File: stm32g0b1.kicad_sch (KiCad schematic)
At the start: 1 part, among them U5 STM32G0B1RETx

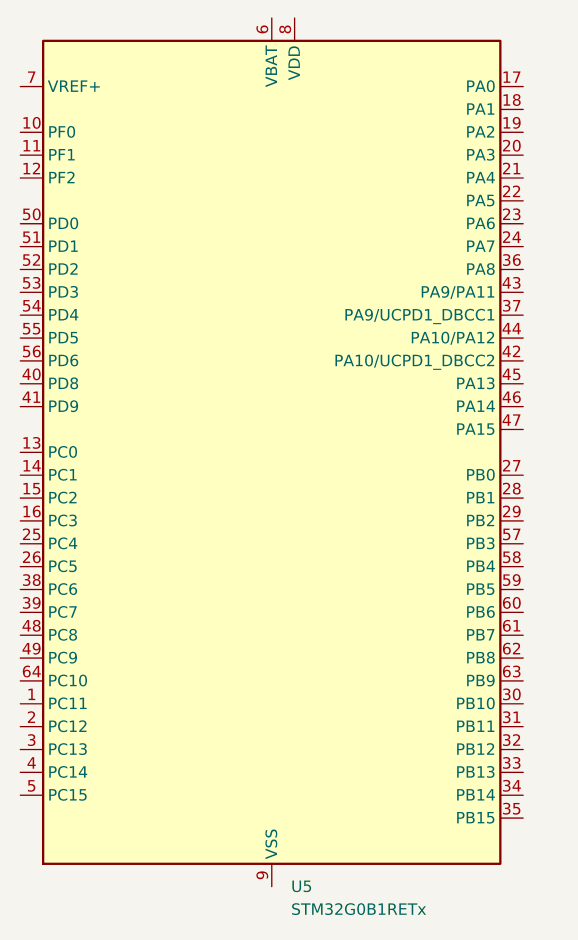
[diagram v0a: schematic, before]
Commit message: fix: added switcher placeholders
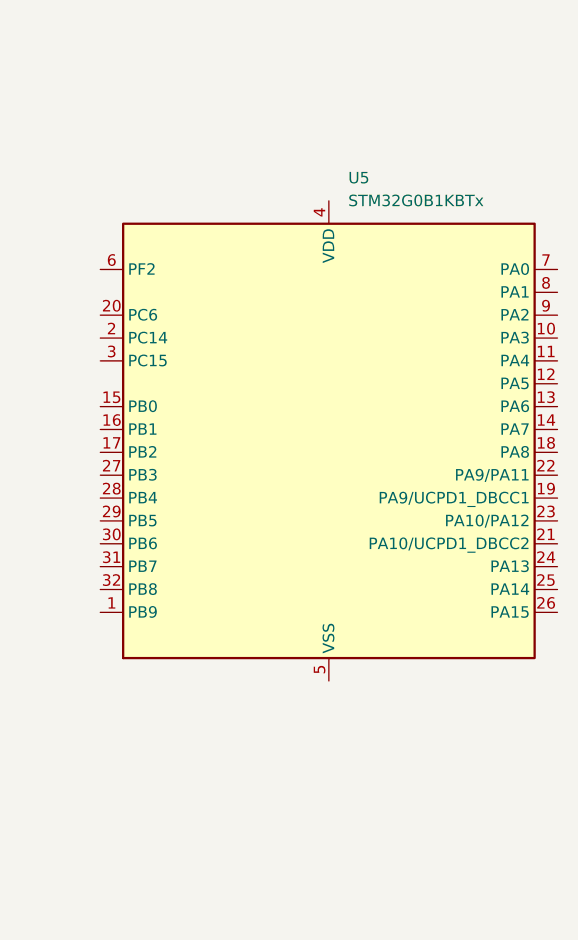
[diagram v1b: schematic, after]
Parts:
- removed U5: STM32G0B1RETx, Package_QFP:LQFP-64_10x10mm_P0.5mm, symbol MCU_ST_STM32G0:STM32G0B1RETx
- added U5: STM32G0B1KBTx, Package_QFP:LQFP-32_7x7mm_P0.8mm, symbol MCU_ST_STM32G0:STM32G0B1KBTx
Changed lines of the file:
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@@
 	(paper "A4")
 	(symbol
-		(lib_id "MCU_ST_STM32G0:STM32G0B1RETx")
-		(at 135.89 96.52 0)
+		(lib_id "MCU_ST_STM32G0:STM32G0B1KBTx")
+		(at 142.24 96.52 0)
 		(unit 1)
 		(exclude_from_sim no)
@@
 		(fields_autoplaced yes)
 		(property "Reference" "U5"
-			(at 138.0333 144.78 0)
+			(at 144.3833 66.04 0)
 			(effects
 				(font
@@
 			)
 		)
-		(property "Value" "STM32G0B1RETx"
-			(at 138.0333 147.32 0)
+		(property "Value" "STM32G0B1KBTx"
+			(at 144.3833 68.58 0)
 			(effects
 				(font
@@
 			)
 		)
-		(property "Footprint" "Package_QFP:LQFP-64_10x10mm_P0.5mm"
-			(at 110.49 142.24 0)
+		(property "Footprint" "Package_QFP:LQFP-32_7x7mm_P0.8mm"
+			(at 119.38 119.38 0)
 			(effects
 				(font
@@
 			)
 		)
-		(property "Datasheet" "https://www.st.com/resource/en/datasheet/stm32g0b1re.pdf"
-			(at 135.89 96.52 0)
+		(property "Datasheet" "https://www.st.com/resource/en/datasheet/stm32g0b1kb.pdf"
+			(at 142.24 96.52 0)
 			(effects
 				(font
@@
 			)
 		)
-		(property "Description" "STMicroelectronics Arm Cortex-M0+ MCU, 512KB flash, 144KB RAM, 64 MHz, 1.7-3.6V, 60 GPIO, LQFP64"
-			(at 135.89 96.52 0)
+		(property "Description" "STMicroelectronics Arm Cortex-M0+ MCU, 128KB flash, 144KB RAM, 64 MHz, 1.7-3.6V, 30 GPIO, LQFP32"
+			(at 142.24 96.52 0)
 			(effects
 				(font
@@
 			)
 		)
-		(pin "7"
-		)
-		(pin "11"
-		)
-		(pin "10"
-		)
-		(pin "5"
-		)
 		(pin "6"
 		)
-		(pin "9"
-		)
-		(pin "8"
-		)
-		(pin "17"
-		)
-		(pin "18"
-		)
-		(pin "19"
-		)
 		(pin "20"
-		)
-		(pin "21"
-		)
-		(pin "22"
-		)
-		(pin "23"
-		)
-		(pin "24"
-		)
-		(pin "36"
-		)
-		(pin "43"
-		)
-		(pin "37"
-		)
-		(pin "44"
-		)
-		(pin "42"
-		)
-		(pin "45"
-		)
-		(pin "46"
-		)
-		(pin "47"
-		)
-		(pin "27"
-		)
-		(pin "28"
-		)
-		(pin "29"
-		)
-		(pin "57"
-		)
-		(pin "58"
-		)
-		(pin "59"
-		)
-		(pin "60"
-		)
-		(pin "61"
-		)
-		(pin "62"
-		)
-		(pin "63"
-		)
-		(pin "30"
-		)
-		(pin "31"
-		)
-		(pin "32"
-		)
-		(pin "33"
-		)
-		(pin "34"
-		)
-		(pin "35"
-		)
-		(pin "12"
-		)
-		(pin "50"
-		)
-		(pin "51"
-		)
-		(pin "52"
-		)
-		(pin "53"
-		)
-		(pin "54"
-		)
-		(pin "55"
-		)
-		(pin "56"
-		)
-		(pin "40"
-		)
-		(pin "41"
-		)
-		(pin "13"
-		)
-		(pin "14"
-		)
-		(pin "15"
-		)
-		(pin "16"
-		)
-		(pin "25"
-		)
-		(pin "26"
-		)
-		(pin "38"
-		)
-		(pin "39"
-		)
-		(pin "48"
-		)
-		(pin "49"
-		)
-		(pin "64"
-		)
-		(pin "1"
 		)
 		(pin "2"
@@
 		(pin "3"
 		)
+		(pin "21"
+		)
+		(pin "25"
+		)
+		(pin "24"
+		)
+		(pin "26"
+		)
+		(pin "15"
+		)
+		(pin "17"
+		)
+		(pin "16"
+		)
+		(pin "29"
+		)
+		(pin "30"
+		)
+		(pin "27"
+		)
+		(pin "1"
+		)
+		(pin "28"
+		)
 		(pin "4"
 		)
+		(pin "31"
+		)
+		(pin "8"
+		)
+		(pin "32"
+		)
+		(pin "9"
+		)
+		(pin "5"
+		)
+		(pin "12"
+		)
+		(pin "7"
+		)
+		(pin "13"
+		)
+		(pin "10"
+		)
+		(pin "22"
+		)
+		(pin "11"
+		)
+		(pin "19"
+		)
+		(pin "14"
+		)
+		(pin "23"
+		)
+		(pin "18"
+		)
 		(instances

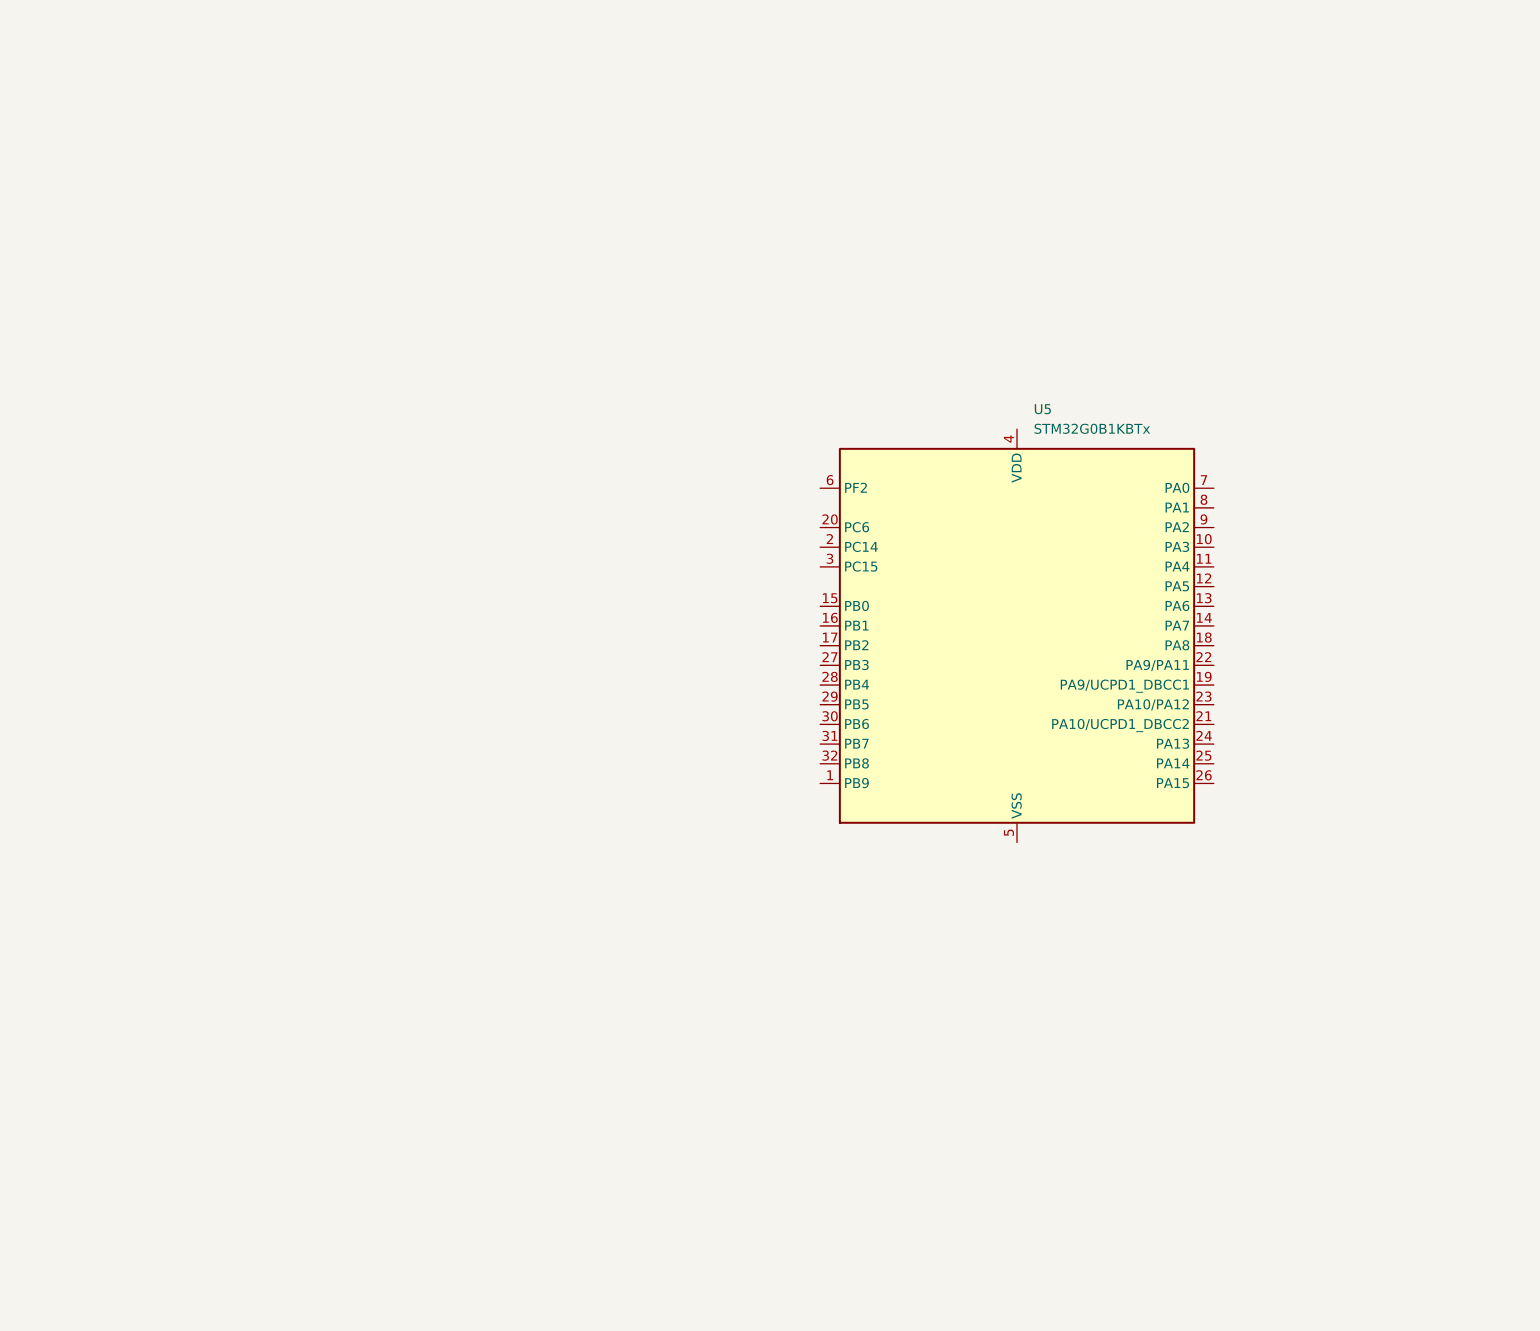
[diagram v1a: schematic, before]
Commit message: feat: done rough board placements for general shape
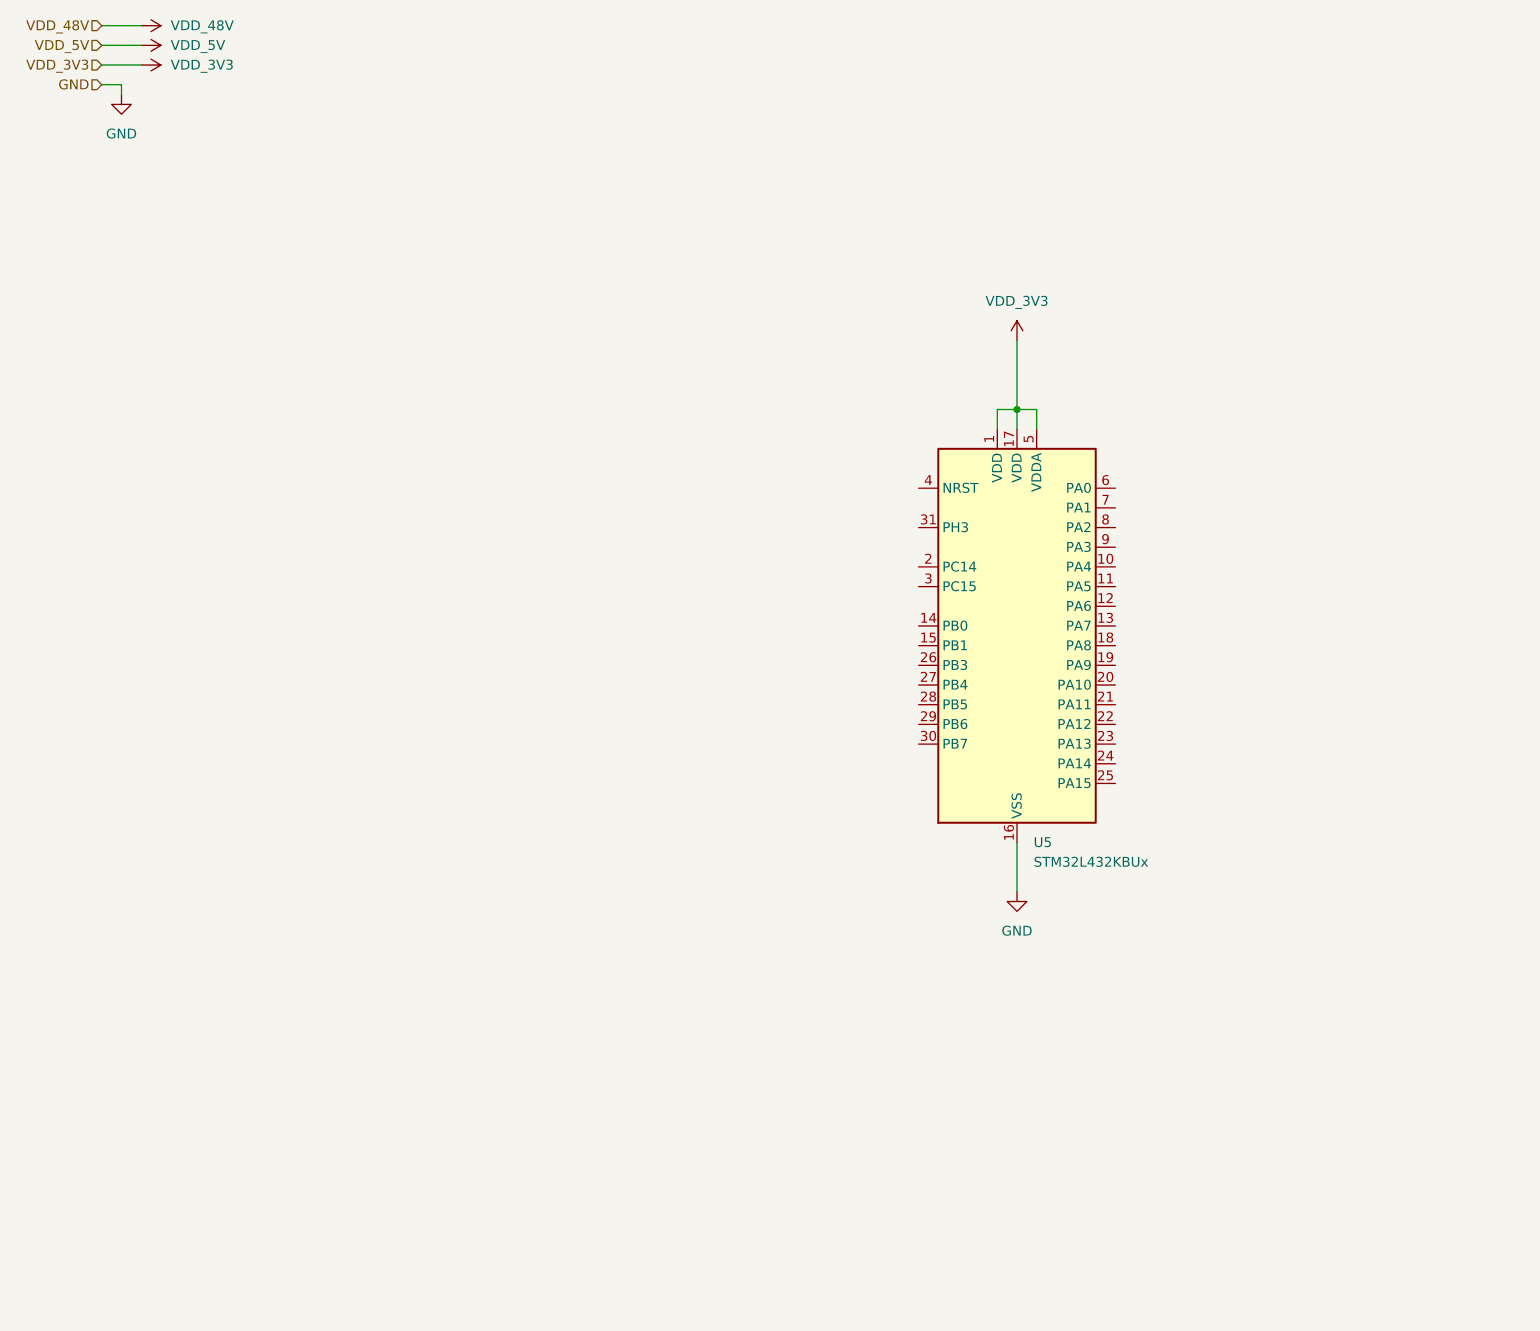
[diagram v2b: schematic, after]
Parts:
- removed U5: STM32G0B1KBTx, Package_QFP:LQFP-32_7x7mm_P0.8mm, symbol MCU_ST_STM32G0:STM32G0B1KBTx
- added U5: STM32L432KBUx, Package_DFN_QFN:QFN-32-1EP_5x5mm_P0.5mm_EP3.45x3.45mm, symbol MCU_ST_STM32L4:STM32L432KBUx
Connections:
- new net GND: U5.16 (VSS), U5.32 (VSS), U5.33 (VSS)
- new net VDD_3V3: U5.1 (VDD), U5.17 (VDD), U5.5 (VDDA)

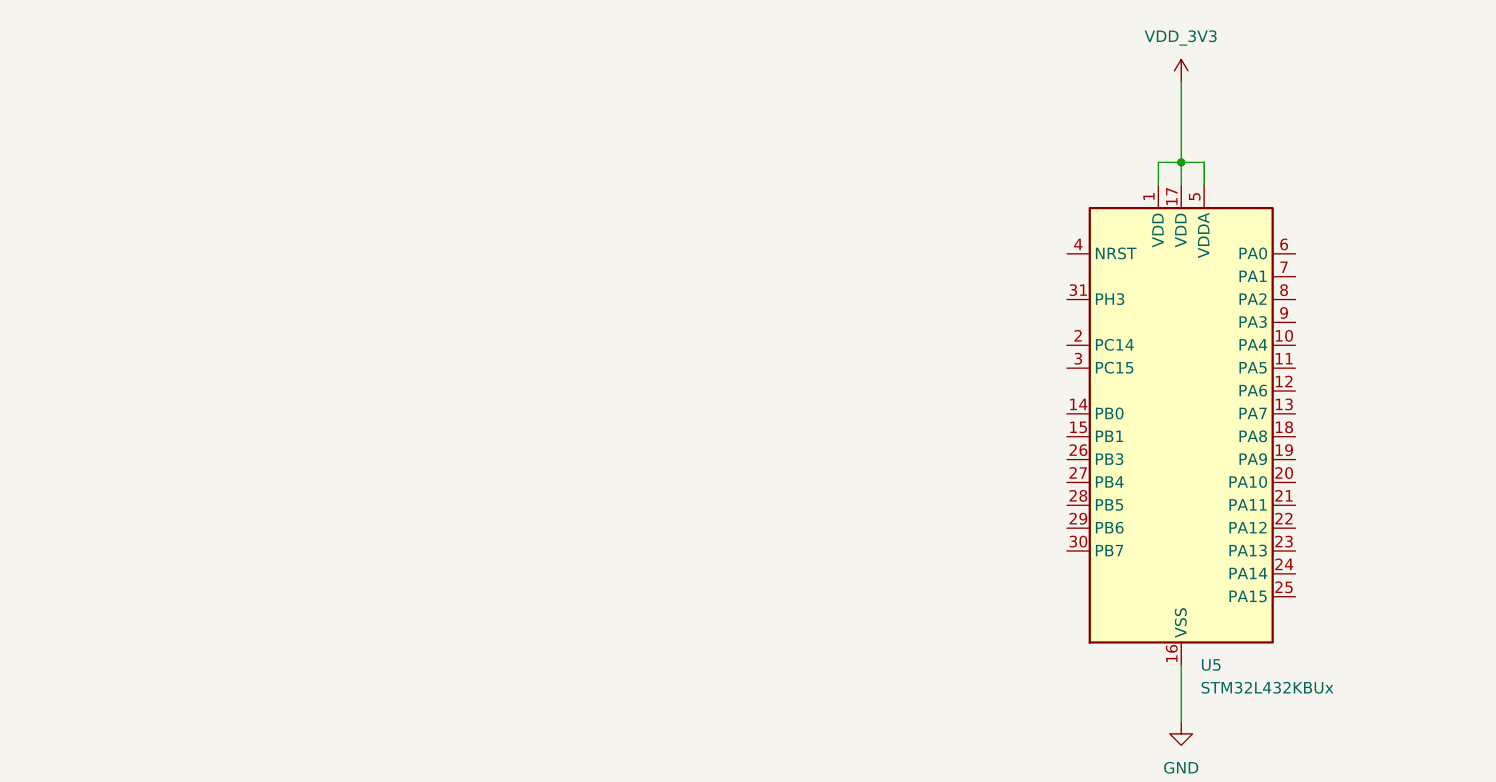
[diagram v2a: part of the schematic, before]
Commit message: fix: added placeholder stlink connector
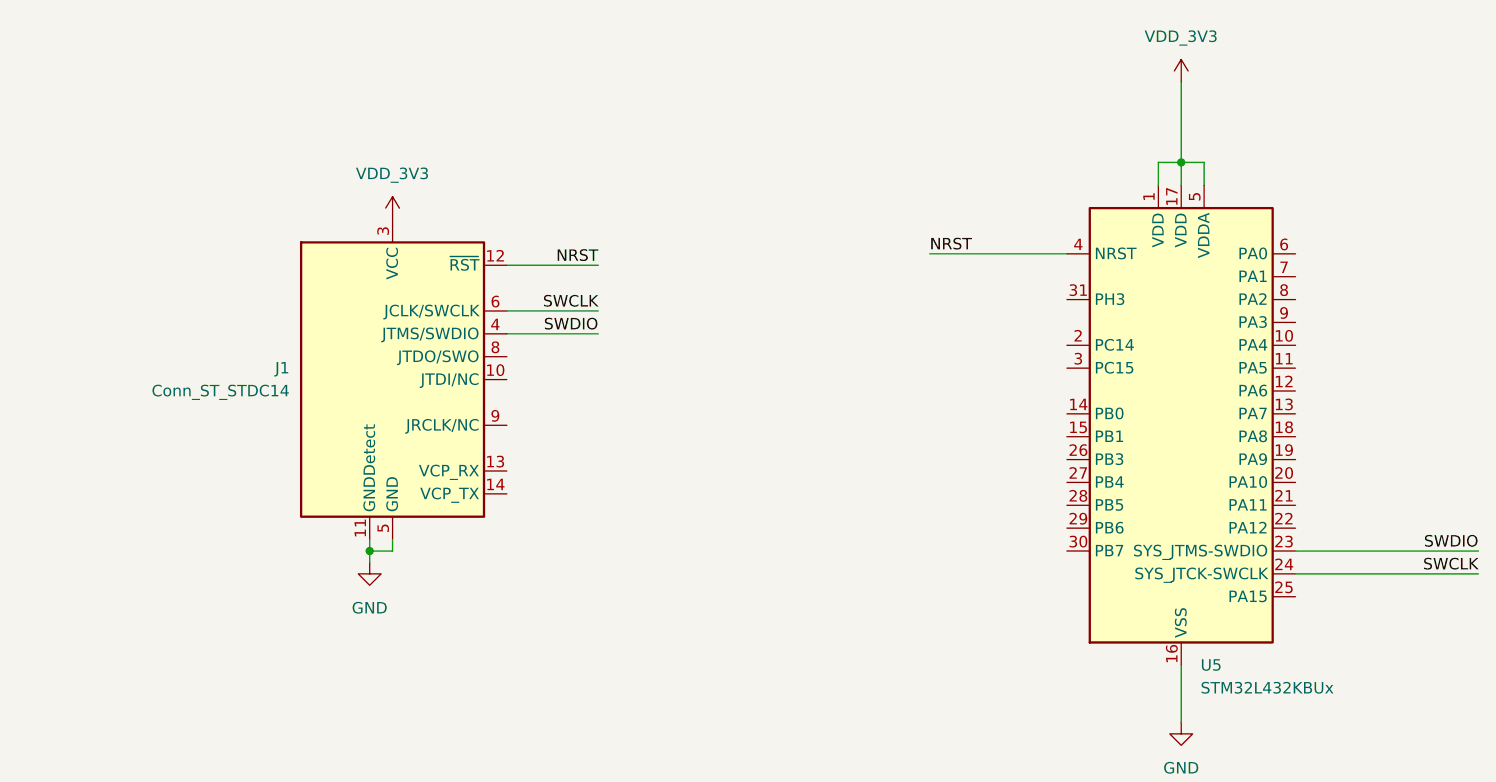
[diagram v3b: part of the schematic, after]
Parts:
- added J1: Conn_ST_STDC14, Connector_PinHeader_1.27mm:PinHeader_2x07_P1.27mm_Vertical_SMD, symbol Connector:Conn_ST_STDC14
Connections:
- net GND: now also J1.11 (GNDDetect), J1.5 (GND), J1.7 (GND)
- net VDD_3V3: now also J1.3 (VCC)
- net SWDIO: now reaches U5.23 (PA13)
- net SWDIO: now also J1.4 (JTMS/SWDIO)
- net SWCLK: now reaches U5.24 (PA14)
- net SWCLK: now also J1.6 (JCLK/SWCLK)
- net NRST: now reaches U5.4 (NRST)
- net NRST: now also J1.12 (~{RST})
